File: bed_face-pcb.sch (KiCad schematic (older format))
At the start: 98 parts, among them SW1 SW_Push, U1 ProMicro

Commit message: re-ordered annotations, begain placing components
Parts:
- D1, D48: footprint (none) -> Keebio-Parts:Diode-Hybrid-Back
- D10: renamed from D37; footprint (none) -> Keebio-Parts:Diode-Hybrid-Back
- D11: renamed from D41; footprint (none) -> Keebio-Parts:Diode-Hybrid-Back
- D12: renamed from D45; footprint (none) -> Keebio-Parts:Diode-Hybrid-Back
- D13: renamed from D2; footprint (none) -> Keebio-Parts:Diode-Hybrid-Back
- D14: renamed from D6; footprint (none) -> Keebio-Parts:Diode-Hybrid-Back
- D15: renamed from D10; footprint (none) -> Keebio-Parts:Diode-Hybrid-Back
- D16: renamed from D14; footprint (none) -> Keebio-Parts:Diode-Hybrid-Back
- D17: renamed from D18; footprint (none) -> Keebio-Parts:Diode-Hybrid-Back
- D18: renamed from D22; footprint (none) -> Keebio-Parts:Diode-Hybrid-Back
- D19: renamed from D26; footprint (none) -> Keebio-Parts:Diode-Hybrid-Back
- D2: renamed from D5; footprint (none) -> Keebio-Parts:Diode-Hybrid-Back
- D20: renamed from D30; footprint (none) -> Keebio-Parts:Diode-Hybrid-Back
- D21: renamed from D34; footprint (none) -> Keebio-Parts:Diode-Hybrid-Back
- D22: renamed from D38; footprint (none) -> Keebio-Parts:Diode-Hybrid-Back
- D23: renamed from D42; footprint (none) -> Keebio-Parts:Diode-Hybrid-Back
- D24: renamed from D46; footprint (none) -> Keebio-Parts:Diode-Hybrid-Back
- D25: renamed from D3; footprint (none) -> Keebio-Parts:Diode-Hybrid-Back
- D26: renamed from D7; footprint (none) -> Keebio-Parts:Diode-Hybrid-Back
- D27: renamed from D11; footprint (none) -> Keebio-Parts:Diode-Hybrid-Back
- D28: renamed from D15; footprint (none) -> Keebio-Parts:Diode-Hybrid-Back
- D29: renamed from D19; footprint (none) -> Keebio-Parts:Diode-Hybrid-Back
- D3: renamed from D9; footprint (none) -> Keebio-Parts:Diode-Hybrid-Back
- D30: renamed from D23; footprint (none) -> Keebio-Parts:Diode-Hybrid-Back
- D31: renamed from D27; footprint (none) -> Keebio-Parts:Diode-Hybrid-Back
- D32: renamed from D31; footprint (none) -> Keebio-Parts:Diode-Hybrid-Back
- D33: renamed from D35; footprint (none) -> Keebio-Parts:Diode-Hybrid-Back
- D34: renamed from D39; footprint (none) -> Keebio-Parts:Diode-Hybrid-Back
- D35: renamed from D43; footprint (none) -> Keebio-Parts:Diode-Hybrid-Back
- D36: renamed from D47; footprint (none) -> Keebio-Parts:Diode-Hybrid-Back
- D37: renamed from D4; footprint (none) -> Keebio-Parts:Diode-Hybrid-Back
- D38: renamed from D8; footprint (none) -> Keebio-Parts:Diode-Hybrid-Back
- D39: renamed from D12; footprint (none) -> Keebio-Parts:Diode-Hybrid-Back
- D4: renamed from D13; footprint (none) -> Keebio-Parts:Diode-Hybrid-Back
- D40: renamed from D16; footprint (none) -> Keebio-Parts:Diode-Hybrid-Back
- D41: renamed from D20; footprint (none) -> Keebio-Parts:Diode-Hybrid-Back
- D42: renamed from D24; footprint (none) -> Keebio-Parts:Diode-Hybrid-Back
- D43: renamed from D28; footprint (none) -> Keebio-Parts:Diode-Hybrid-Back
- D44: renamed from D32; footprint (none) -> Keebio-Parts:Diode-Hybrid-Back
- D45: renamed from D36; footprint (none) -> Keebio-Parts:Diode-Hybrid-Back
- D46: renamed from D40; footprint (none) -> Keebio-Parts:Diode-Hybrid-Back
- D47: renamed from D44; footprint (none) -> Keebio-Parts:Diode-Hybrid-Back
- D5: renamed from D17; footprint (none) -> Keebio-Parts:Diode-Hybrid-Back
- D6: renamed from D21; footprint (none) -> Keebio-Parts:Diode-Hybrid-Back
- D7: renamed from D25; footprint (none) -> Keebio-Parts:Diode-Hybrid-Back
- D8: renamed from D29; footprint (none) -> Keebio-Parts:Diode-Hybrid-Back
- D9: renamed from D33; footprint (none) -> Keebio-Parts:Diode-Hybrid-Back
- MX1, MX48: footprint (none) -> MX_Only:MXOnly-1U-NoLED
- MX10: renamed from MX37; footprint (none) -> MX_Only:MXOnly-1U-NoLED
- MX11: renamed from MX41; footprint (none) -> MX_Only:MXOnly-1U-NoLED
- MX12: renamed from MX45; footprint (none) -> MX_Only:MXOnly-1U-NoLED
- MX13: renamed from MX2; footprint (none) -> MX_Only:MXOnly-1U-NoLED
- MX14: renamed from MX6; footprint (none) -> MX_Only:MXOnly-1U-NoLED
- MX15: renamed from MX10; footprint (none) -> MX_Only:MXOnly-1U-NoLED
- MX16: renamed from MX14; footprint (none) -> MX_Only:MXOnly-1U-NoLED
- MX17: renamed from MX18; footprint (none) -> MX_Only:MXOnly-1U-NoLED
- MX18: renamed from MX22; footprint (none) -> MX_Only:MXOnly-1U-NoLED
- MX19: renamed from MX26; footprint (none) -> MX_Only:MXOnly-1U-NoLED
- MX2: renamed from MX5; footprint (none) -> MX_Only:MXOnly-1U-NoLED
- MX20: renamed from MX30; footprint (none) -> MX_Only:MXOnly-1U-NoLED
- MX21: renamed from MX34; footprint (none) -> MX_Only:MXOnly-1U-NoLED
- MX22: renamed from MX38; footprint (none) -> MX_Only:MXOnly-1U-NoLED
- MX23: renamed from MX42; footprint (none) -> MX_Only:MXOnly-1U-NoLED
- MX24: renamed from MX46; value \\ | -> ' \"; footprint (none) -> MX_Only:MXOnly-1U-NoLED
- MX25: renamed from MX3; footprint (none) -> MX_Only:MXOnly-1U
- MX26: renamed from MX7; footprint (none) -> MX_Only:MXOnly-1U-NoLED
- MX27: renamed from MX11; footprint (none) -> MX_Only:MXOnly-1U-NoLED
- MX28: renamed from MX15; footprint (none) -> MX_Only:MXOnly-1U-NoLED
- MX29: renamed from MX19; footprint (none) -> MX_Only:MXOnly-1U-NoLED
- MX3: renamed from MX9; footprint (none) -> MX_Only:MXOnly-1U-NoLED
- MX30: renamed from MX23; footprint (none) -> MX_Only:MXOnly-1U-NoLED
- MX31: renamed from MX27; footprint (none) -> MX_Only:MXOnly-1U-NoLED
- MX32: renamed from MX31; footprint (none) -> MX_Only:MXOnly-1U-NoLED
- MX33: renamed from MX35; footprint (none) -> MX_Only:MXOnly-1U-NoLED
- MX34: renamed from MX39; footprint (none) -> MX_Only:MXOnly-1U-NoLED
- MX35: renamed from MX43; footprint (none) -> MX_Only:MXOnly-1U-NoLED
- MX36: renamed from MX47; footprint (none) -> MX_Only:MXOnly-1U-NoLED
- MX37: renamed from MX4; footprint (none) -> MX_Only:MXOnly-1U-NoLED
- MX38: renamed from MX8; footprint (none) -> MX_Only:MXOnly-1U-NoLED
- MX39: renamed from MX12; footprint (none) -> MX_Only:MXOnly-1U-NoLED
- MX4: renamed from MX13; footprint (none) -> MX_Only:MXOnly-1U-NoLED
- MX40: renamed from MX16; footprint (none) -> MX_Only:MXOnly-1U-NoLED
- MX41: renamed from MX20; footprint (none) -> MX_Only:MXOnly-1U-NoLED
- MX42: renamed from MX24; footprint (none) -> MX_Only:MXOnly-1U-NoLED
- MX43: renamed from MX28; footprint (none) -> MX_Only:MXOnly-1U-NoLED
- MX44: renamed from MX32; footprint (none) -> MX_Only:MXOnly-1U-NoLED
- MX45: renamed from MX36; footprint (none) -> MX_Only:MXOnly-1U-NoLED
- MX46: renamed from MX40; footprint (none) -> MX_Only:MXOnly-1U-NoLED
- MX47: renamed from MX44; footprint (none) -> MX_Only:MXOnly-1U-NoLED
- MX5: renamed from MX17; footprint (none) -> MX_Only:MXOnly-1U-NoLED
- MX6: renamed from MX21; footprint (none) -> MX_Only:MXOnly-1U-NoLED
- MX7: renamed from MX25; footprint (none) -> MX_Only:MXOnly-1U-NoLED
- MX8: renamed from MX29; footprint (none) -> MX_Only:MXOnly-1U-NoLED
- MX9: renamed from MX33; footprint (none) -> MX_Only:MXOnly-1U-NoLED
- SW1: footprint (none) -> random-keyboard-parts:PushButton_6x6mm_TH_Pretty
- U1: footprint (none) -> Keebio-Parts:ArduinoProMicro-BackSide

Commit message: styled switch footprints, initial pcb placement
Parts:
- MX1, MX10, MX11, MX12, MX13, MX14, MX15, MX16, MX17, MX18, MX19, MX2, MX20, MX21, MX22, MX23, MX24, MX26, MX27, MX28, MX29, MX3, MX30, MX31, MX32, MX33, MX34, MX35, MX36, MX37, MX38, MX39, MX4, MX40, MX41, MX42, MX43, MX44, MX45, MX46, MX47, MX48, MX5, MX6, MX7, MX8, MX9: footprint MX_Only:MXOnly-1U-NoLED -> MX_Only:MXOnly-1U-NoLED-EDIT
- MX25: footprint MX_Only:MXOnly-1U -> MX_Only:MXOnly-1U-EDIT
- SW1: footprint random-keyboard-parts:PushButton_6x6mm_TH_Pretty -> Keebio-Parts:SW_Tactile_SPST_Angled_MJTP1117

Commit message: added +5V, GND to Power net w/ 15 mil track width
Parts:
- U1: footprint Keebio-Parts:ArduinoProMicro-BackSide -> promicro:ProMicro
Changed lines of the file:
@@
 F 0 "U1" H 2600 3287 60  0000 C CNN
 F 1 "ProMicro" H 2600 3181 60  0000 C CNN
-F 2 "Keebio-Parts:ArduinoProMicro-BackSide" H 2700 1200 60  0001 C CNN
+F 2 "promicro:ProMicro" H 2700 1200 60  0001 C CNN
 F 3 "" H 2700 1200 60  0000 C CNN
 	1    2600 2250

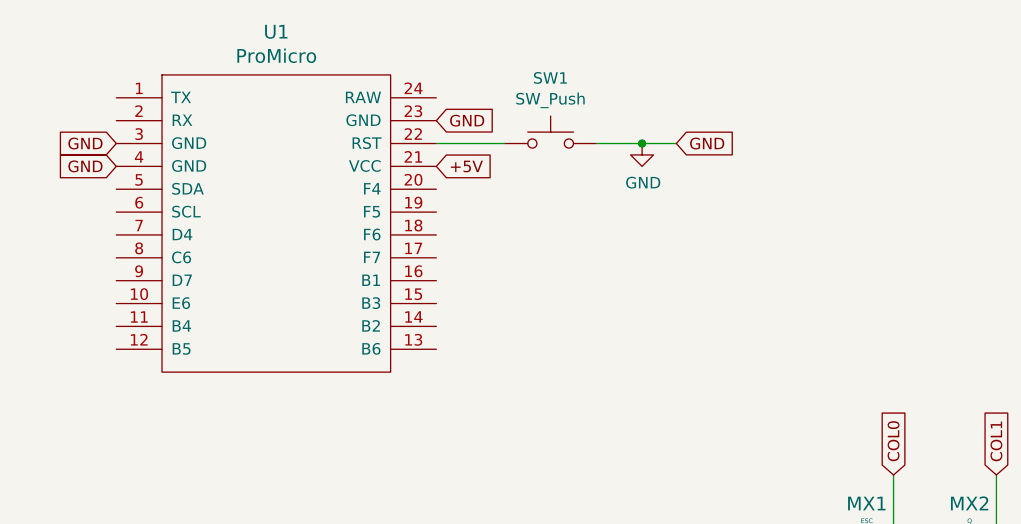
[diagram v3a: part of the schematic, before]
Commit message: matrix routed, GND fill placed * still needs resistor for LED? * need to add silkscreen/graphic
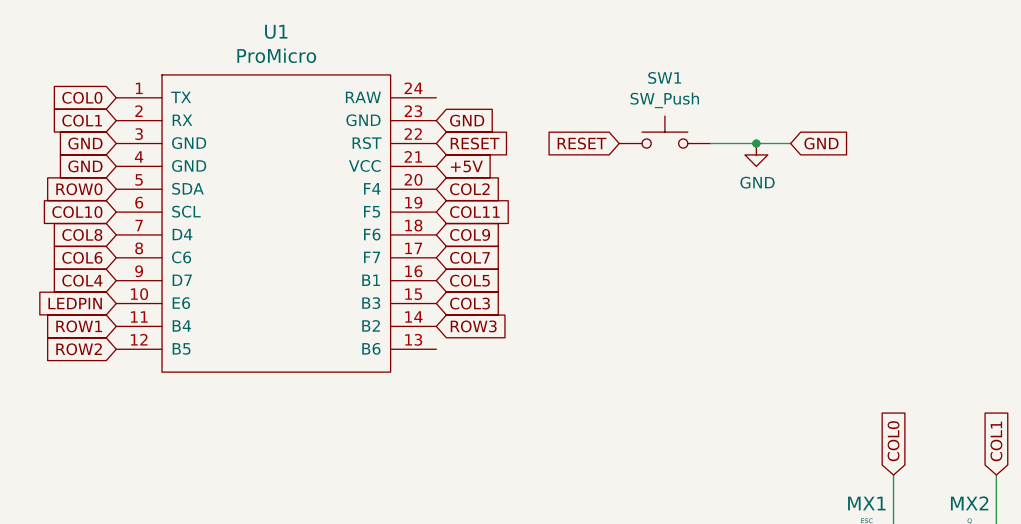
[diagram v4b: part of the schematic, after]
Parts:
- U1: footprint promicro:ProMicro -> Keebio-Parts:ArduinoProMicro-BackSide
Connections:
- net COL0: now also U1.1 (TX)
- net COL1: now also U1.2 (RX)
- net COL10: now also U1.6 (SCL)
- net COL11: now also U1.19 (F5)
- net COL2: now also U1.20 (F4)
- net COL3: now also U1.15 (B3)
- net COL4: now also U1.9 (D7)
- net COL5: now also U1.16 (B1)
- net COL6: now also U1.8 (C6)
- net COL7: now also U1.17 (F7)
- net COL8: now also U1.7 (D4)
- net COL9: now also U1.18 (F6)
- net LEDPIN: now also U1.10 (E6)
- net ROW0: now also U1.5 (SDA)
- net ROW1: now also U1.11 (B4)
- net ROW2: now also U1.12 (B5)
- net ROW3: now also U1.14 (B2)
- net RESET: now reaches SW1.1, U1.22 (RST)
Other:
- moved on the sheet: SW1
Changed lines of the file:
@@
 F 0 "U1" H 2600 3287 60  0000 C CNN
 F 1 "ProMicro" H 2600 3181 60  0000 C CNN
-F 2 "promicro:ProMicro" H 2700 1200 60  0001 C CNN
+F 2 "Keebio-Parts:ArduinoProMicro-BackSide" H 2700 1200 60  0001 C CNN
 F 3 "" H 2700 1200 60  0000 C CNN
 	1    2600 2250
@@
 L Switch:SW_Push SW1
 U 1 1 646D85CB
-P 3800 1700
-F 0 "SW1" H 3800 1985 50  0000 C CNN
-F 1 "SW_Push" H 3800 1894 50  0000 C CNN
-F 2 "Keebio-Parts:SW_Tactile_SPST_Angled_MJTP1117" H 3800 1900 50  0001 C CNN
-F 3 "~" H 3800 1900 50  0001 C CNN
-	1    3800 1700
-	1    0    0    -1
-$EndComp
-Wire Wire Line
-	3300 1700 3600 1700
-Wire Wire Line
-	4000 1700 4200 1700
+P 4300 1700
+F 0 "SW1" H 4300 1985 50  0000 C CNN
+F 1 "SW_Push" H 4300 1894 50  0000 C CNN
+F 2 "Keebio-Parts:SW_Tactile_SPST_Angled_MJTP1117" H 4300 1900 50  0001 C CNN
+F 3 "~" H 4300 1900 50  0001 C CNN
+	1    4300 1700
+	1    0    0    -1
+$EndComp
+Wire Wire Line
+	4500 1700 4700 1700
 $Comp
 L power:GND #PWR01
 U 1 1 646DAA7E
-P 4200 1700
-F 0 "#PWR01" H 4200 1450 50  0001 C CNN
-F 1 "GND" H 4205 1527 50  0000 C CNN
-F 2 "" H 4200 1700 50  0001 C CNN
-F 3 "" H 4200 1700 50  0001 C CNN
-	1    4200 1700
-	1    0    0    -1
-$EndComp
-Wire Wire Line
-	4200 1700 4350 1700
-Connection ~ 4200 1700
-Text GLabel 4350 1700 2    50   Input ~ 0
+P 4700 1700
+F 0 "#PWR01" H 4700 1450 50  0001 C CNN
+F 1 "GND" H 4705 1527 50  0000 C CNN
+F 2 "" H 4700 1700 50  0001 C CNN
+F 3 "" H 4700 1700 50  0001 C CNN
+	1    4700 1700
+	1    0    0    -1
+$EndComp
+Wire Wire Line
+	4700 1700 4850 1700
+Connection ~ 4700 1700
+Text GLabel 4850 1700 2    50   Input ~ 0
 GND
 $Comp
@@
 Text GLabel 10500 3850 2    50   Input ~ 0
 ROW0
+Text GLabel 1900 1900 0    50   Input ~ 0
+ROW0
+Text GLabel 1900 1600 0    50   Input ~ 0
+COL1
+Text GLabel 1900 2500 0    50   Input ~ 0
+ROW1
+Text GLabel 1900 2600 0    50   Input ~ 0
+ROW2
+Text GLabel 3300 2500 2    50   Input ~ 0
+ROW3
+Text GLabel 3300 2400 2    50   Input ~ 0
+COL3
+Text GLabel 3300 1900 2    50   Input ~ 0
+COL2
+Text GLabel 1900 2300 0    50   Input ~ 0
+COL4
+Text GLabel 3300 2300 2    50   Input ~ 0
+COL5
+Text GLabel 1900 2200 0    50   Input ~ 0
+COL6
+Text GLabel 3300 2200 2    50   Input ~ 0
+COL7
+Text GLabel 1900 2100 0    50   Input ~ 0
+COL8
+Text GLabel 3300 2100 2    50   Input ~ 0
+COL9
+Text GLabel 1900 2000 0    50   Input ~ 0
+COL10
+Text GLabel 3300 2000 2    50   Input ~ 0
+COL11
+Text GLabel 1900 1500 0    50   Input ~ 0
+COL0
+Text GLabel 1900 2400 0    50   Input ~ 0
+LEDPIN
+Text GLabel 4100 1700 0    50   Input ~ 0
+RESET
+Text GLabel 3300 1700 2    50   Input ~ 0
+RESET
 $EndSCHEMATC

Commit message: added split vs. 2u space
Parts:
- MX42: footprint MX_Only:MXOnly-1U-NoLED-EDIT -> MX_Only:MXOnly-2U-ReversedStabilizers-NoLED-ComboSpace-EDIT
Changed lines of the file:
@@
 F 0 "MX42" H 7433 5823 60  0000 C CNN
 F 1 "LSPACE" H 7433 5749 20  0000 C CNN
-F 2 "MX_Only:MXOnly-1U-NoLED-EDIT" H 6775 5575 60  0001 C CNN
+F 2 "MX_Only:MXOnly-2U-ReversedStabilizers-NoLED-ComboSpace-EDIT" H 6775 5575 60  0001 C CNN
 F 3 "" H 6775 5575 60  0001 C CNN
 	1    7400 5600

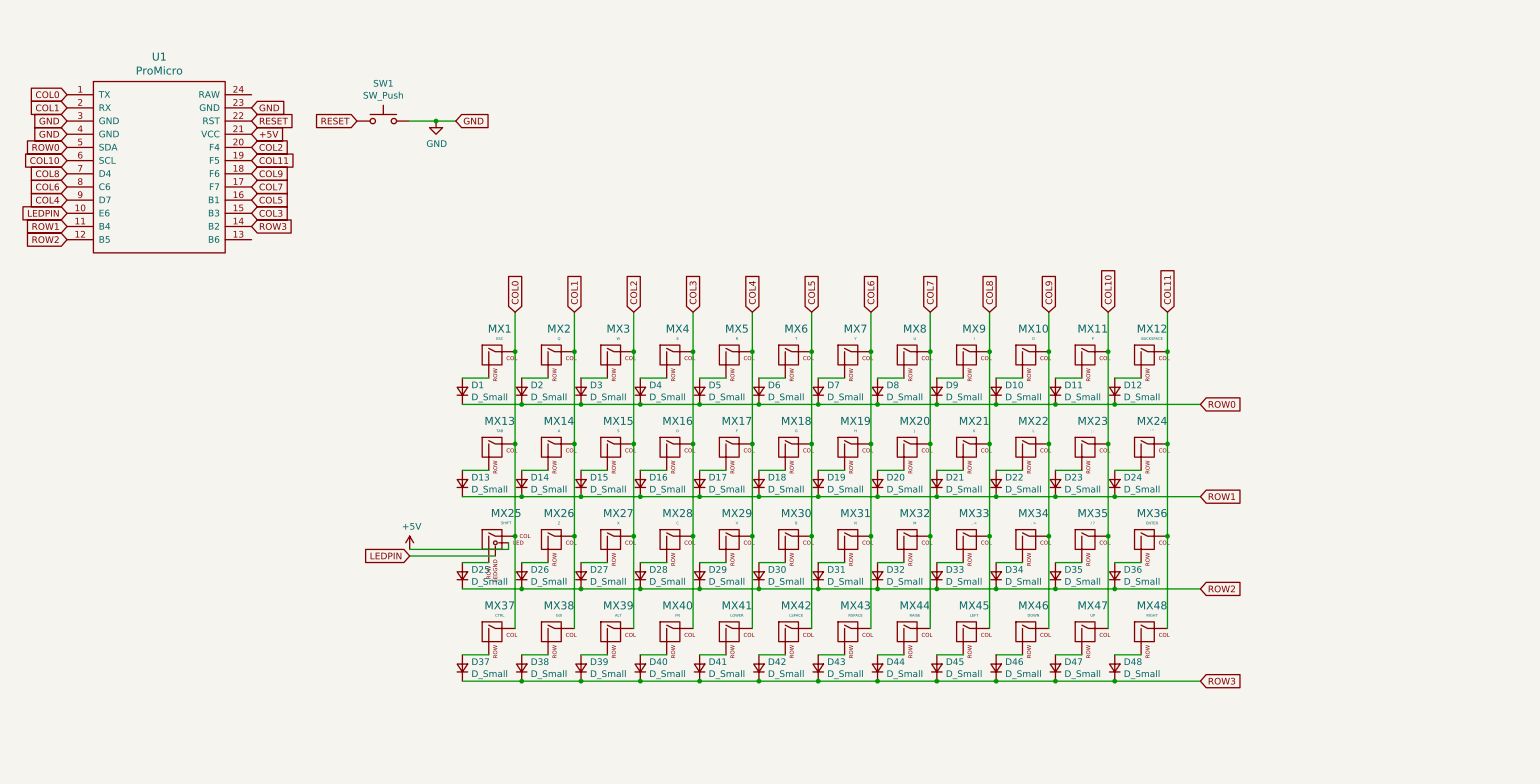
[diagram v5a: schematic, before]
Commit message: began placing encoders, squaring matrix * squaring matrix gains MCU pins * RE footpints need silkscreen changes
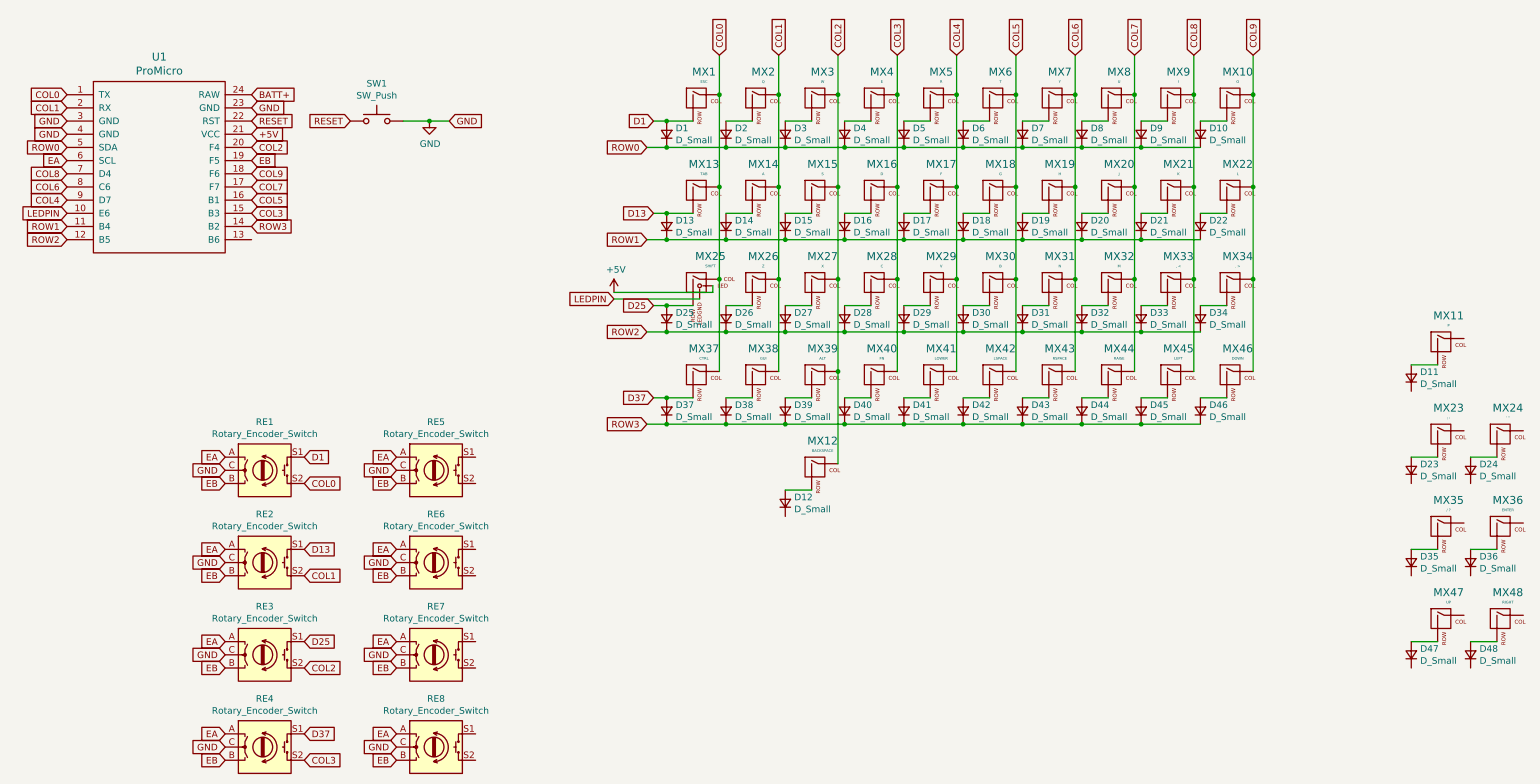
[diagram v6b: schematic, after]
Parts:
- added RE1, RE2, RE3, RE4, RE5, RE6, RE7, RE8: Rotary_Encoder_Switch, reversible-kicad-footprints:MX-1U-EC11_Switch, symbol Device:Rotary_Encoder_Switch
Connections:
- net COL0: now also RE1.S2
- net COL1: now also RE2.S2
- net COL2: now also MX12.1 (COL), RE3.S2
- net COL3: now also RE4.S2
- net GND: now also RE1.C, RE2.C, RE3.C, RE4.C, RE5.C, RE6.C, RE7.C, RE8.C
- net ROW0: no longer D11.1 (K), D12.1 (K)
- net ROW1: no longer D23.1 (K), D24.1 (K)
- net ROW2: no longer D35.1 (K), D36.1 (K)
- net ROW3: no longer D47.1 (K), D48.1 (K)
- net BATT+: now reaches U1.24 (RAW)
- net D1: now reaches D1.2 (A), MX1.2 (ROW)
- net D1: now also RE1.S1
- net D13: now reaches D13.2 (A), MX13.2 (ROW)
- net D13: now also RE2.S1
- net D37: now reaches D37.2 (A), MX37.2 (ROW)
- net D37: now also RE4.S1
- net D25: now reaches D25.2 (A), MX25.2 (ROW)
- net D25: now also RE3.S1
- removed net COL10: MX11.1 (COL), MX23.1 (COL), MX35.1 (COL), MX47.1 (COL), U1.6 (SCL)
- removed net COL11: MX12.1 (COL), MX24.1 (COL), MX36.1 (COL), MX48.1 (COL), U1.19 (F5)
- new net EA: RE1.A, RE2.A, RE3.A, RE4.A, RE5.A, RE6.A, RE7.A, RE8.A, U1.6 (SCL)
- new net EB: RE1.B, RE2.B, RE3.B, RE4.B, RE5.B, RE6.B, RE7.B, RE8.B, U1.19 (F5)
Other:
- moved on the sheet: D1, D10, D11, D12, D13, D14, D15, D16, D17, D18, D19, D2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

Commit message: squared up matrix, placed + tracked encoders * encoder support for first and last columns * needs battery connector * encoder silks need changing
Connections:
- net COL0: now also RE2.S2, RE3.S2, RE4.S2
- net COL1: no longer RE2.S2
- net COL2: now also RE5.S2; no longer RE3.S2
- net COL3: now also MX11.1 (COL); no longer RE4.S2
- net COL4: now also MX23.1 (COL)
- net COL5: now also MX24.1 (COL), RE6.S2
- net COL6: now also MX36.1 (COL), RE7.S2
- net COL7: now also MX35.1 (COL)
- net COL8: now also MX48.1 (COL), RE8.S2
- net COL9: now also MX47.1 (COL)
- net ROW4: now reaches U1.13 (B6)
- net ROW4: now also D11.1 (K), D12.1 (K), D23.1 (K), D24.1 (K), D35.1 (K), D36.1 (K), D47.1 (K), D48.1 (K)
- net D12: now reaches D12.2 (A), MX12.2 (ROW)
- net D12: now also RE5.S1
- net D24: now reaches D24.2 (A), MX24.2 (ROW)
- net D24: now also RE6.S1
- net D36: now reaches D36.2 (A), MX36.2 (ROW)
- net D36: now also RE7.S1
- net D48: now reaches D48.2 (A), MX48.2 (ROW)
- net D48: now also RE8.S1
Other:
- moved on the sheet: D11, D23, D24, D35, D36, D47, D48, MX11, MX23, MX24, MX35, MX36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
